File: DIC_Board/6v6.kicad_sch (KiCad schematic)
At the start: 8 parts, among them J30 0430450200, U30 TPS27S100APWPR

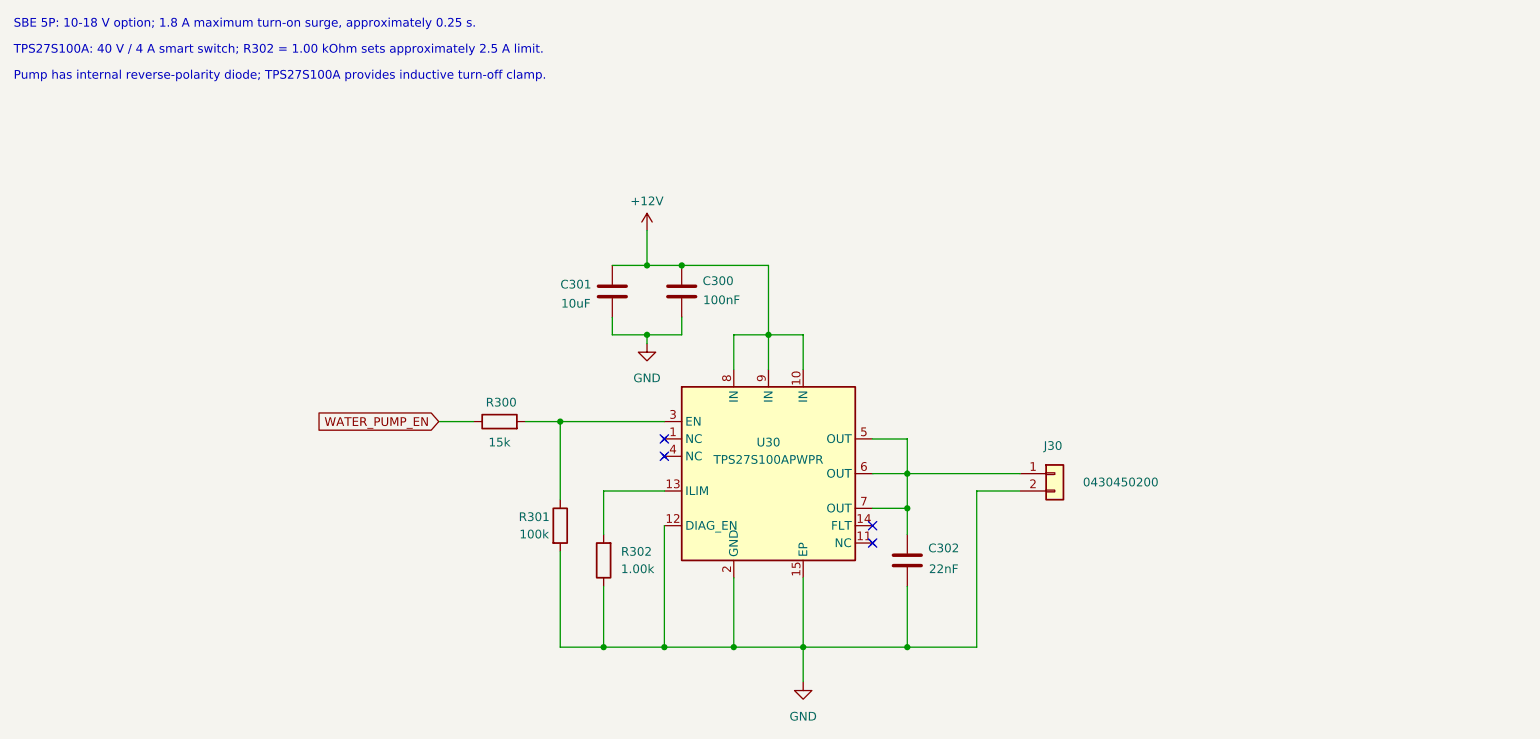
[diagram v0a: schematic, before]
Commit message: Separated the power sheets, did the sensor sheets.
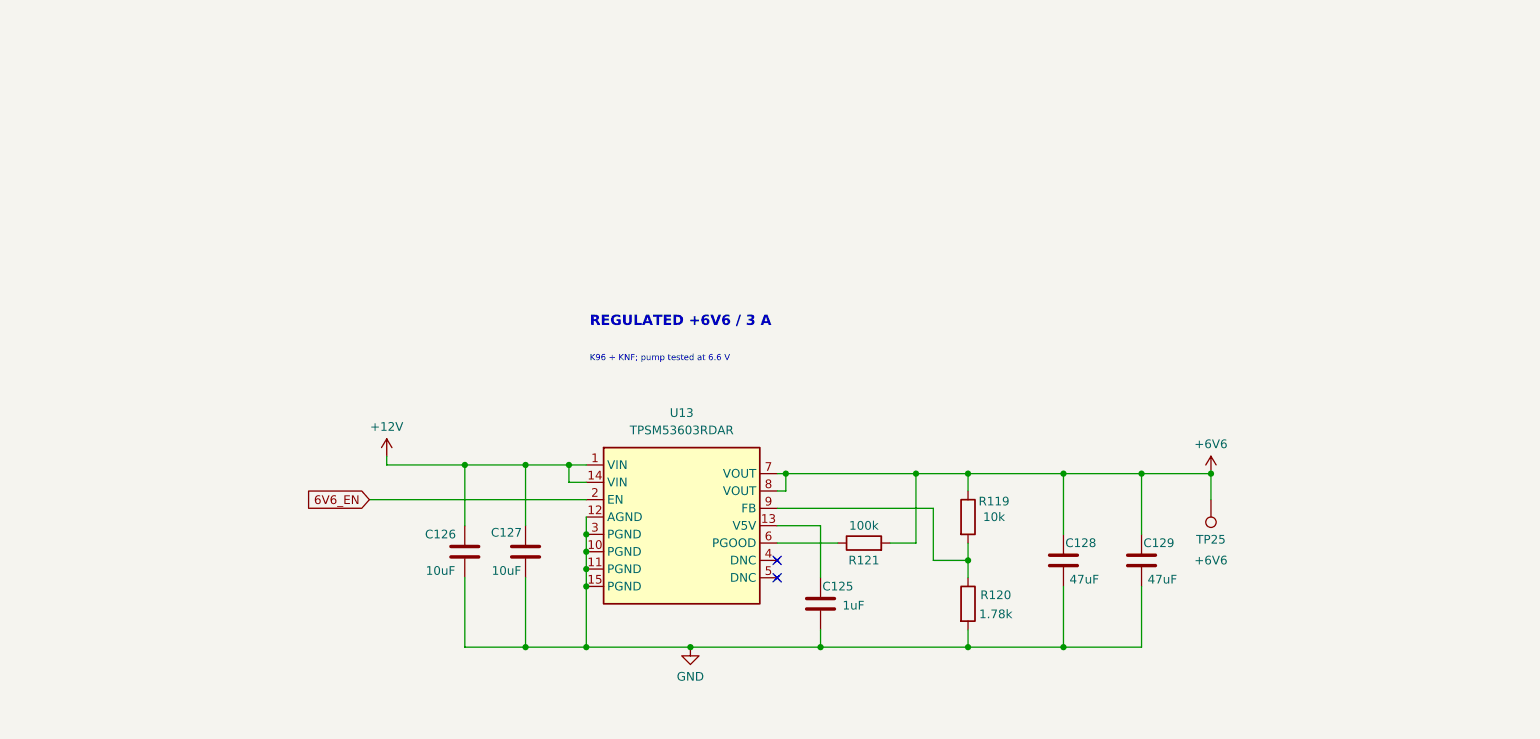
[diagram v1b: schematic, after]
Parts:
- removed C300: 100nF, Capacitor_SMD:C_0402_1005Metric, symbol Device:C
- removed C301: 10uF, Capacitor_SMD:C_1206_3216Metric, symbol Device:C
- removed C302: 22nF, Capacitor_SMD:C_0402_1005Metric, symbol Device:C
- removed J30: 0430450200, Connector_Molex:Molex_Micro-Fit_3.0_43045-0200_2x01_P3.00mm_Horizontal, symbol Connector_Generic:Conn_01x02
- removed R300: 15k, Resistor_SMD:R_0402_1005Metric, symbol Device:R
- removed R301: 100k, Resistor_SMD:R_0402_1005Metric, symbol Device:R
- removed R302: 1.00k, Resistor_SMD:R_0402_1005Metric, symbol Device:R
- removed U30: TPS27S100APWPR, Package_SO:Texas_HTSSOP-14-1EP_4.4x5mm_P0.65mm_EP3.4x5mm_Mask3.155x3.255mm_ThermalVias, symbol DIC_Board:TPS27S100A
- added C125: 1uF, Capacitor_SMD:C_0603_1608Metric, symbol Device:C
- added C126, C127: 10uF, Capacitor_SMD:C_1206_3216Metric, symbol Device:C
- added C128, C129: 47uF, Capacitor_SMD:C_1210_3225Metric, symbol Device:C
- added R119: 10k, Resistor_SMD:R_0402_1005Metric, symbol Device:R
- added R120: 1.78k, Resistor_SMD:R_0402_1005Metric, symbol Device:R
- added R121: 100k, Resistor_SMD:R_0402_1005Metric, symbol Device:R
- added TP25: +6V6, TestPoint:TestPoint_Plated_Hole_D2.0mm, symbol Connector:TestPoint
- added U13: TPSM53603RDAR, Package_DFN_QFN:Texas_B3QFN-14-1EP_5x5.5mm_P0.65mm_ThermalVia, symbol DIC_Board:TPSM53603RDA
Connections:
- net +12V: now also C126.1, C127.1, U13.1 (VIN), U13.14 (VIN)
- net GND: now also C125.2, C126.2, C127.2, C128.2, C129.2, R120.2, U13.10 (PGND), U13.11 (PGND), U13.12 (AGND), U13.15 (PGND), U13.3 (PGND)
- new net: R119.2, R120.1, U13.9 (FB)
- new net: R121.1, U13.6 (PGOOD)
- new net: C125.1, U13.13 (V5V)
- new net +6V6: C128.1, C129.1, R119.1, R121.2, TP25.1, U13.7 (VOUT), U13.8 (VOUT)
- new net 6V6_EN: U13.2 (EN)
- no-connect marks 4 -> 2
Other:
- note added: "K96 + KNF; pump tested at 6.6 V"
- note added: "REGULATED +6V6 / 3 A"
- note removed: "Pump has internal reverse-polarity diode; TPS27S100A provides inductive turn-off clamp."
- note removed: "SBE 5P: 10-18 V option; 1.8 A maximum turn-on surge, approximately 0.25 s."
- note removed: "TPS27S100A: 40 V / 4 A smart switch; R302 = 1.00 kOhm sets approximately 2.5 A limit."
- title: Water Pump -> (none)

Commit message: Synchronize schematic hierarchy and MCU pin map
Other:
- note added: "K96 + KNF; pump tested at 6.6 V; default-on, MCU-controllable"
- note removed: "K96 + KNF; pump tested at 6.6 V"
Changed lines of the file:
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@@
 		)
 	)
-	(text "K96 + KNF; pump tested at 6.6 V"
+	(text "K96 + KNF; pump tested at 6.6 V; default-on, MCU-controllable"
 		(exclude_from_sim no)
 		(at 113.538 72.644 0)
@@
 		)
 	)
-	(global_label "6V6_EN"
+	(hierarchical_label "6V6_EN"
 		(shape input)
 		(at 81.28 92.71 180)
-		(fields_autoplaced yes)
 		(effects
 			(font
@@
 			(justify right)
 		)
-		(property "Intersheetrefs" "${INTERSHEET_REFS}"
-			(at 71.3401 92.71 0)
-			(hide yes)
-			(show_name no)
-			(do_not_autoplace no)
-			(effects
-				(font
-					(size 1.27 1.27)
-				)
-				(justify right)
-			)
-		)
-	)
+	)

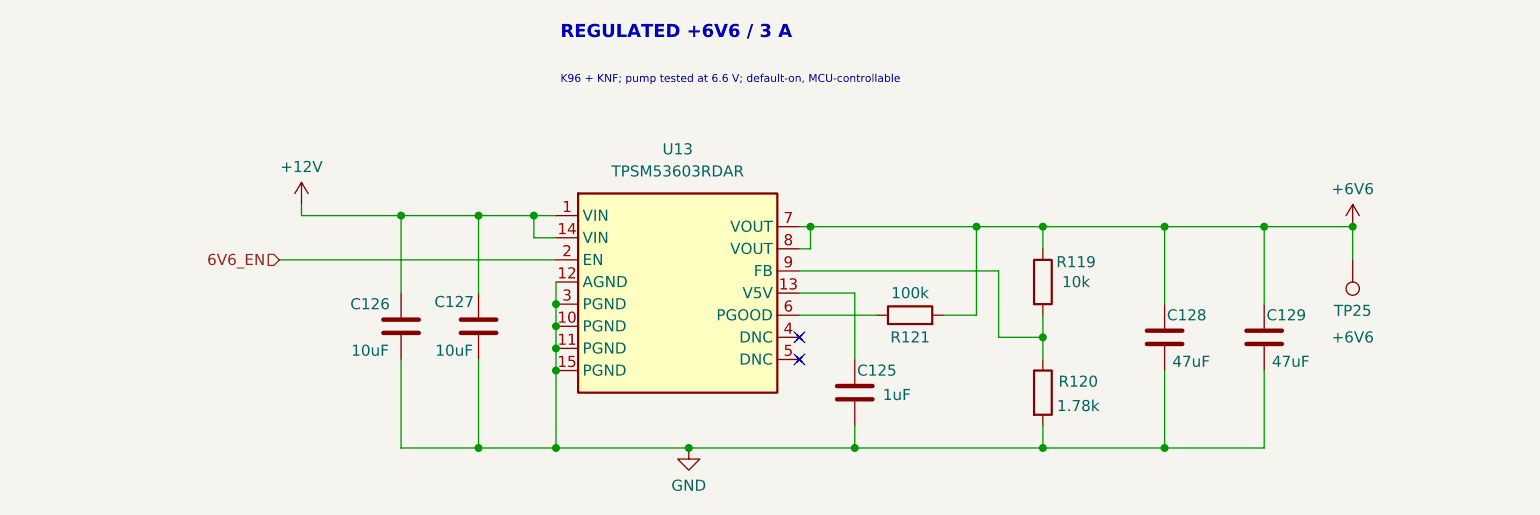
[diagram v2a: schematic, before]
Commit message: Synchronize power, communications, and MCU configuration
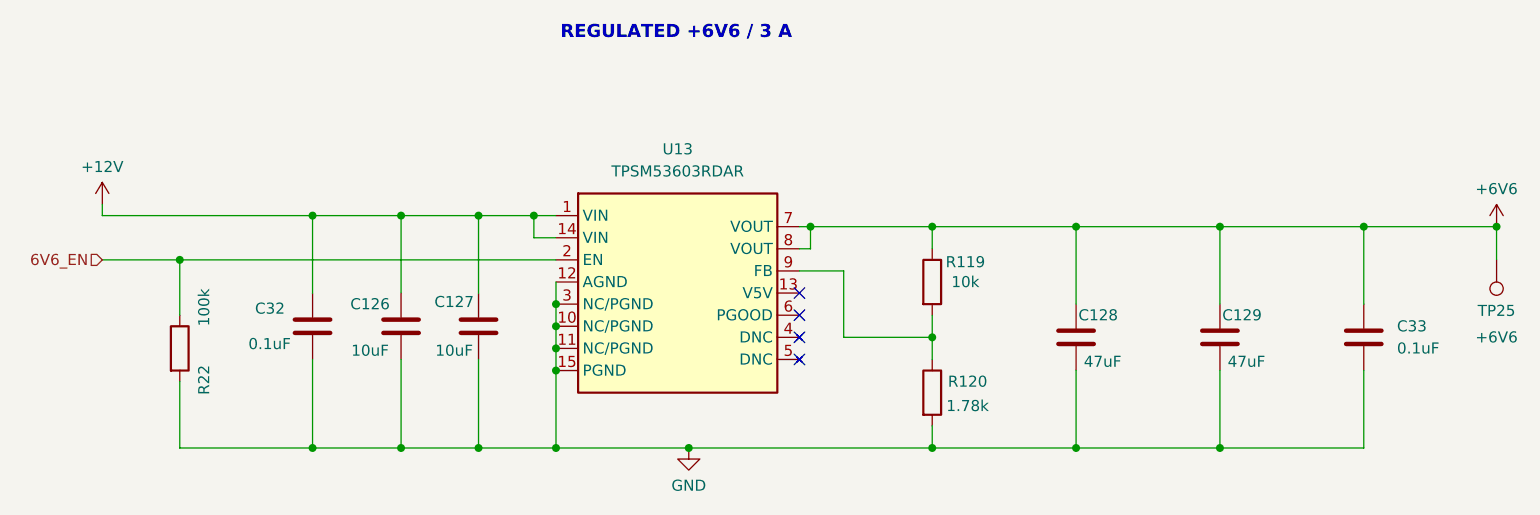
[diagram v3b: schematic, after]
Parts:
- removed C125: 1uF, Capacitor_SMD:C_0603_1608Metric, symbol Device:C
- removed R121: 100k, Resistor_SMD:R_0402_1005Metric, symbol Device:R
- added C32, C33: 0.1uF, symbol Device:C
- added R22: 100k, Resistor_SMD:R_0402_1005Metric, symbol Device:R
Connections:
- net +12V: now also C32.1
- net +6V6: now also C33.1
- net 6V6_EN: now also R22.1
- net GND: now also C32.2, C33.2, R22.2
- no-connect marks 2 -> 4
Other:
- note removed: "K96 + KNF; pump tested at 6.6 V; default-on, MCU-controllable"
- moved on the sheet: C128, C129, R119, R120, TP25

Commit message: Updated board for layout! All footprints added
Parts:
- added C903: 180uF 16V, Capacitor_SMD:CP_Elec_6.3x5.9, symbol Device:C_Polarized
- C32, C33: footprint (none) -> Capacitor_SMD:C_0603_1608Metric; BOM Source (none) -> https://product.tdk.com/en/search/capacitor/ceramic/mlcc/in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; Dielectric (none) -> X7R; MPN (none) -> C1608X7R1H104K080AA; Manufacturer (none) -> TDK; Tolerance (none) -> 10%; Voltage Rating (none) -> 50V
- TP25: now left out of the parts list
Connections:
- net +6V6: now also C903.1
- net GND: now also C903.2
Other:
- note added: "Output bulk"
- moved on the sheet: TP25

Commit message: Let gpt6 astra have a go at routing. bad results.
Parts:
- TP25: footprint TestPoint:TestPoint_Plated_Hole_D2.0mm -> TestPoint:TestPoint_Pad_D1.0mm
- U13: footprint Package_DFN_QFN:Texas_B3QFN-14-1EP_5x5.5mm_P0.65mm_ThermalVia -> DIC_Board:TPSM53603_Thermal_Drill0p3
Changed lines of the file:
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@@
 			)
 		)
-		(property "Footprint" "Package_DFN_QFN:Texas_B3QFN-14-1EP_5x5.5mm_P0.65mm_ThermalVia"
+		(property "Footprint" "DIC_Board:TPSM53603_Thermal_Drill0p3"
 			(at 127 96.52 0)
 			(hide yes)
@@
 			)
 		)
-		(property "Footprint" "TestPoint:TestPoint_Plated_Hole_D2.0mm"
+		(property "Footprint" "TestPoint:TestPoint_Pad_D1.0mm"
 			(at 247.65 92.71 0)
 			(hide yes)
